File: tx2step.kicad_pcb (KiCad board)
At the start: 2 copper layers, 86.4 x 31.8 mm, 60 parts, among them CON1 BARREL_JACK, IC1 TPS2113A, IC3 MCP73831, IC4 TPS61202, IC5 DRV8834, IC6 DRV8834, J1 8P8C, J2 6P4Cx2, J4 Prog, J5 CHASSIS_SWITCHES, SW1 SW_DIP_x02, U1 ATmega328P-MMH, Y1 16 MHz

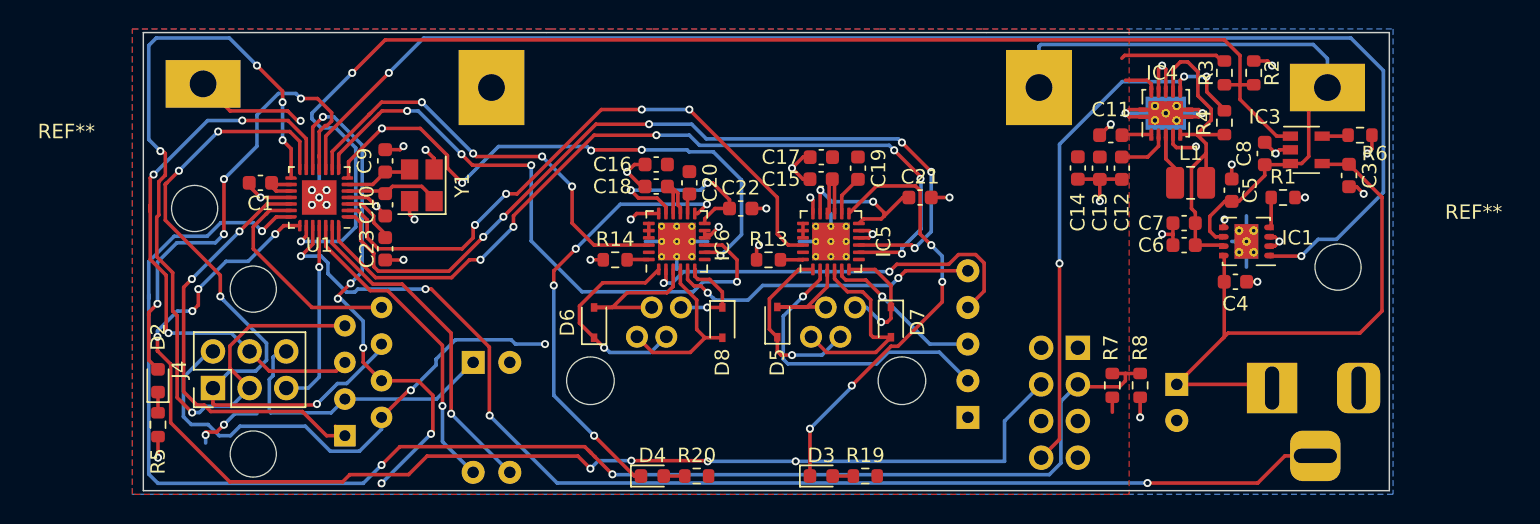
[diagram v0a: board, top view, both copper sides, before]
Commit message: Use trimpots to adjust current clamping
It turns out resistor networks aren't available in a wide variety of
values. Replace the resistor network with fixed value resistors and
add trimpots for each axis to adjust the current clamping.
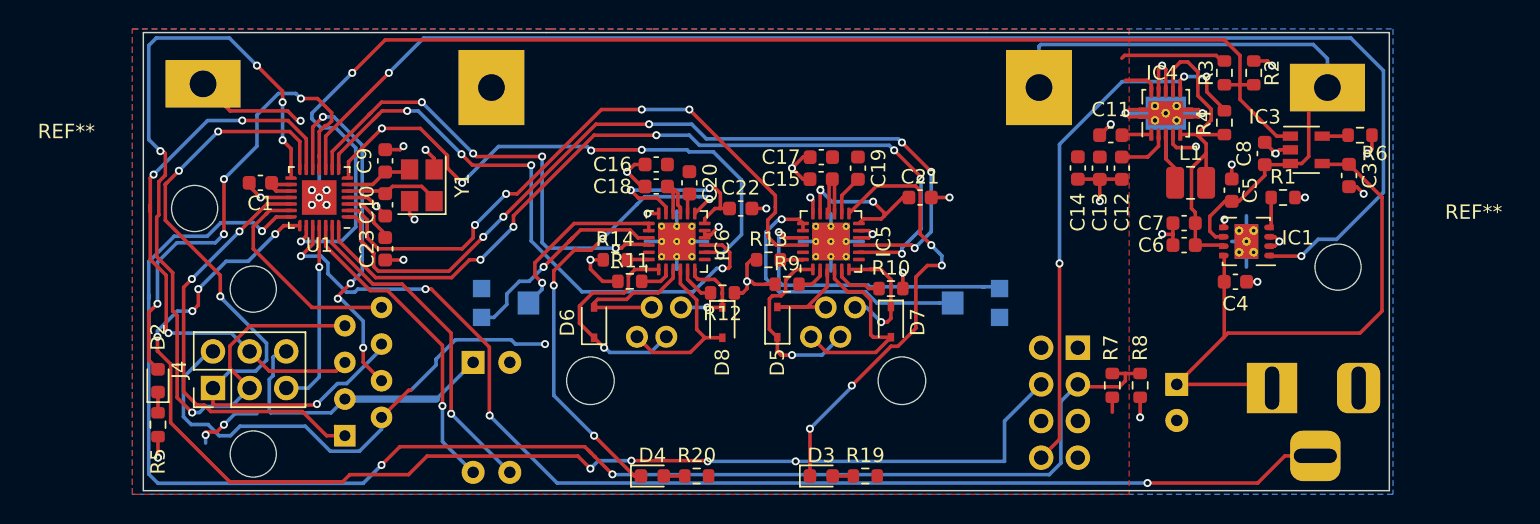
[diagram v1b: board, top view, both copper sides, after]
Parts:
- removed RN1: R_Network04, Resistor_THT:R_Array_SIP5
- added R10: BISEN, Resistor_SMD:R_0603_1608Metric, F.Cu at (160.3, 75.4)
- added R11: AISEN, Resistor_SMD:R_0603_1608Metric, F.Cu at (142.2, 74.9)
- added R12: BISEN, Resistor_SMD:R_0603_1608Metric, F.Cu at (148.6, 75.7)
- added R9: AISEN, Resistor_SMD:R_0603_1608Metric, F.Cu at (153.1, 75.1)
- added RV1: R_POT_TRIM, Potentiometer_SMD:Potentiometer_Bourns_TC33X_Vertical, B.Cu at (166.0, 76.4)
- added RV2: R_POT_TRIM, Potentiometer_SMD:Potentiometer_Bourns_TC33X_Vertical, B.Cu at (133.7, 76.4)
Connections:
- IC5 pad 21: Net-(IC5-Pad19) -> Net-(IC5-Pad21)
- IC6 pad 21: Net-(IC6-Pad19) -> Net-(IC6-Pad21)
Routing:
- net Net-(IC6-Pad2): track 27.8 -> 2.29 mm, vias 2 -> 0
- net Net-(IC5-Pad21): track 0.00 -> 20.9 mm, vias 0 -> 1
- net Net-(IC5-Pad19): track 1.00 -> 20.4 mm, vias 0 -> 1
- net Net-(IC5-Pad2): track 21.4 -> 2.16 mm, vias 1 -> 0
- net Net-(IC6-Pad5): track 21.6 -> 3.13 mm, vias 2 -> 0
- net Net-(IC6-Pad21): track 0.00 -> 15.1 mm, vias 0 -> 1
- net GND: track 124.4 -> 138.4 mm, vias 42 -> 43
- net Net-(IC6-Pad19): track 1.00 -> 12.9 mm, vias 0 -> 1
- net /ST4_RA+: track 37.7 -> 26.0 mm, vias 6 -> 4
- net Net-(IC5-Pad5): track 11.2 -> 3.43 mm, vias 1 -> 0
- net /DEC_PWR: track 30.4 -> 32.6 mm
- net /DEC_DIR: track 43.2 -> 41.9 mm
- net Net-(D4-Pad1): track 30.6 -> 31.6 mm
- net /RA_PWR: track 43.2 -> 44.2 mm
- net Net-(D7-Pad1): track 8.67 -> 9.44 mm
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
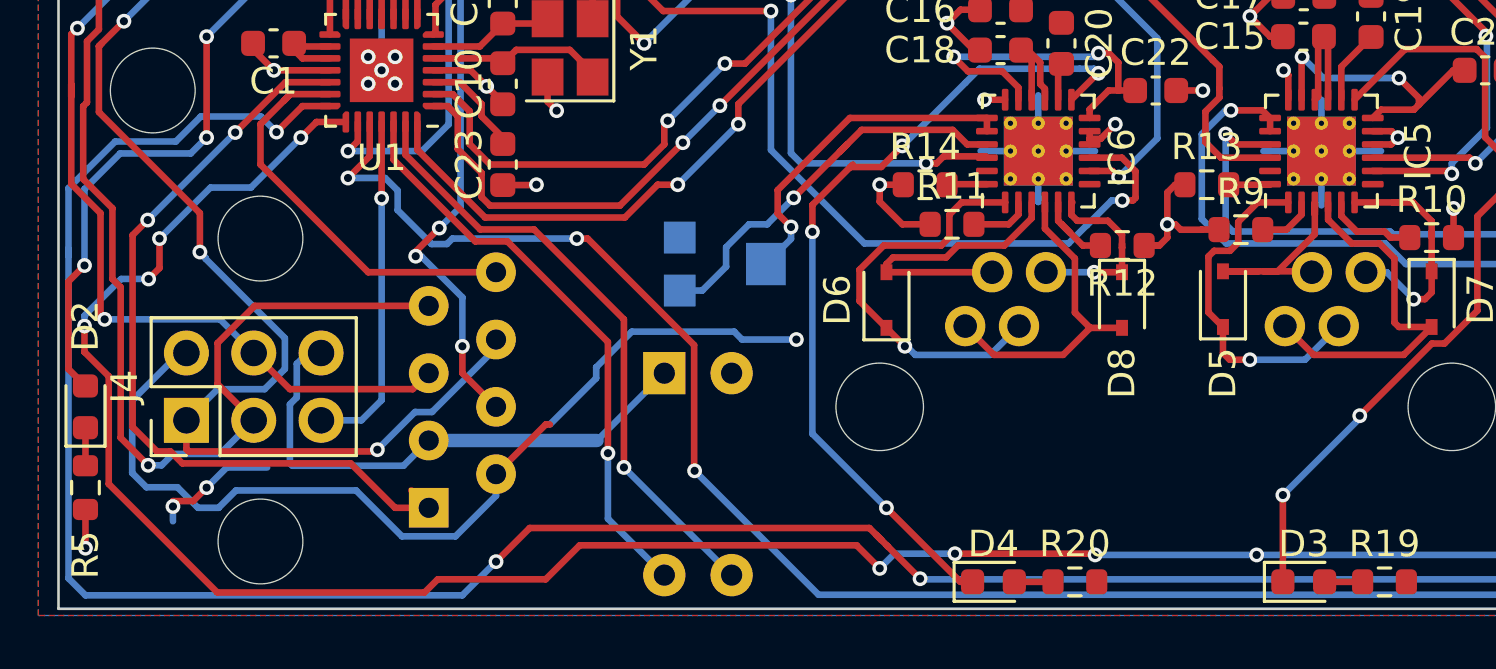
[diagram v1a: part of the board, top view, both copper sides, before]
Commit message: Fix up silkscreen collisions
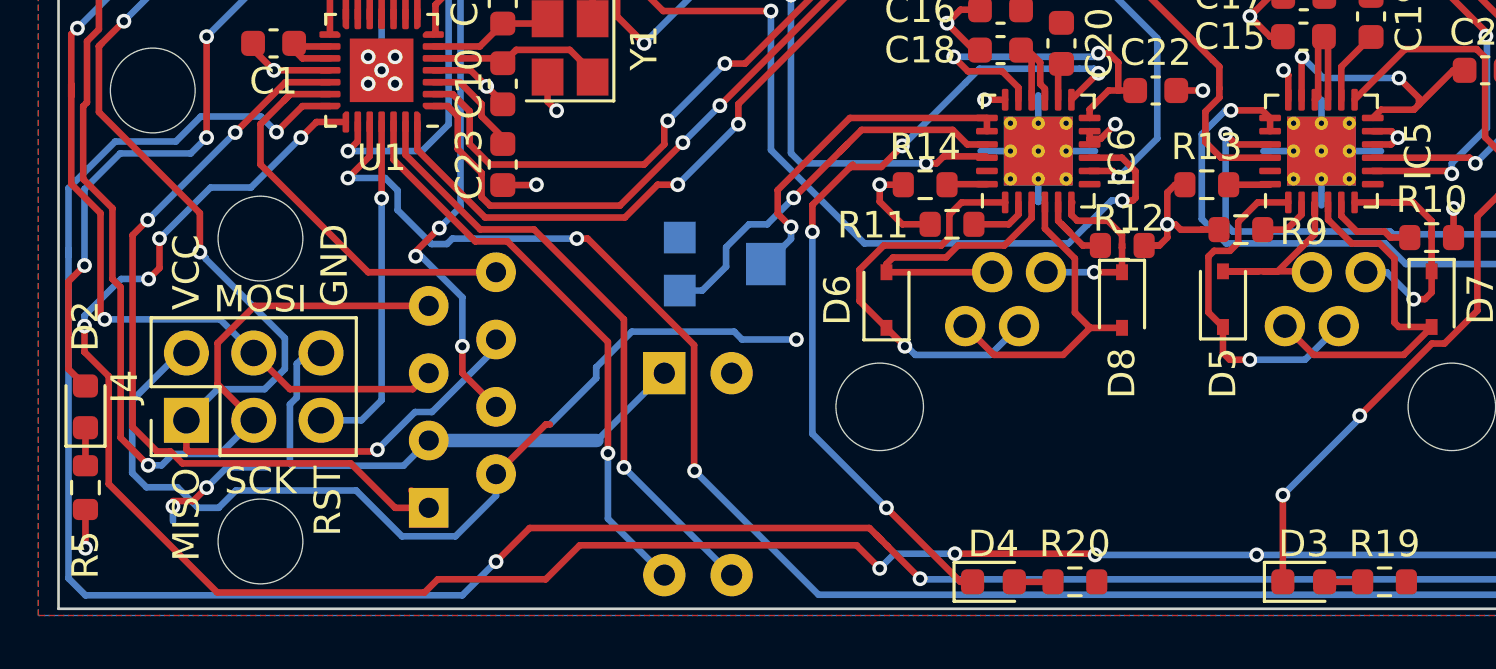
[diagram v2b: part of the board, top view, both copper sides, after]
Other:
- board text added: "GND"
- board text added: "MISO"
- board text added: "MOSI"
- board text added: "RST"
- board text added: "SCK"
- board text added: "VCC"

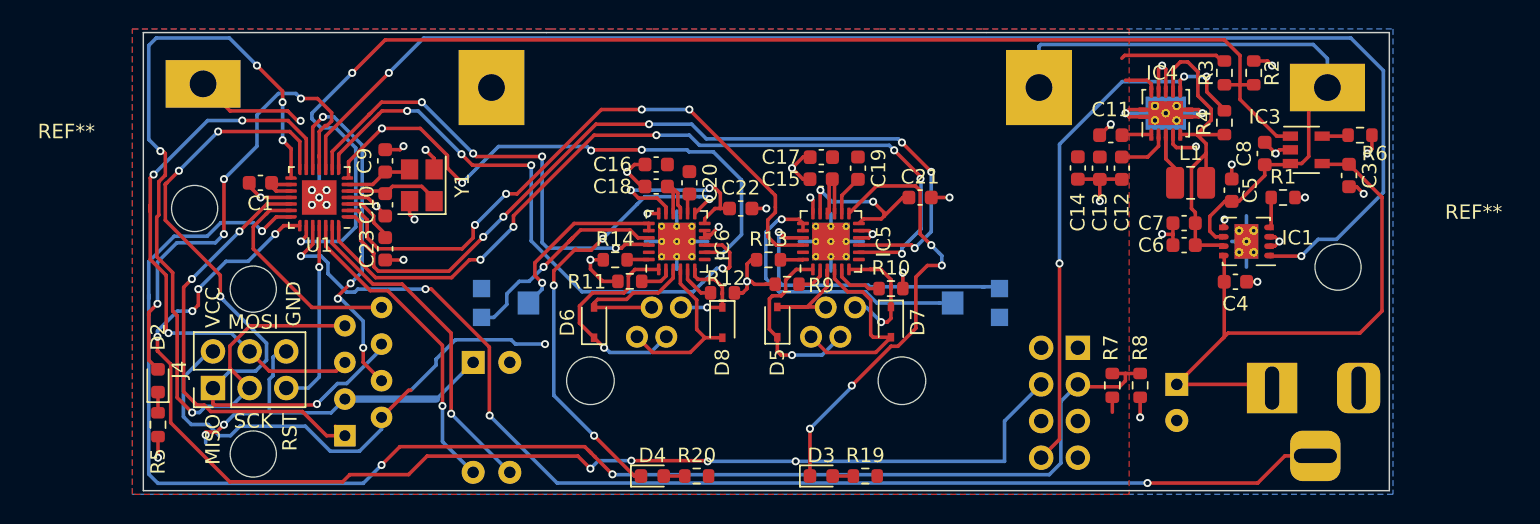
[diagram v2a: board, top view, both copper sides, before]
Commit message: Add more power planes
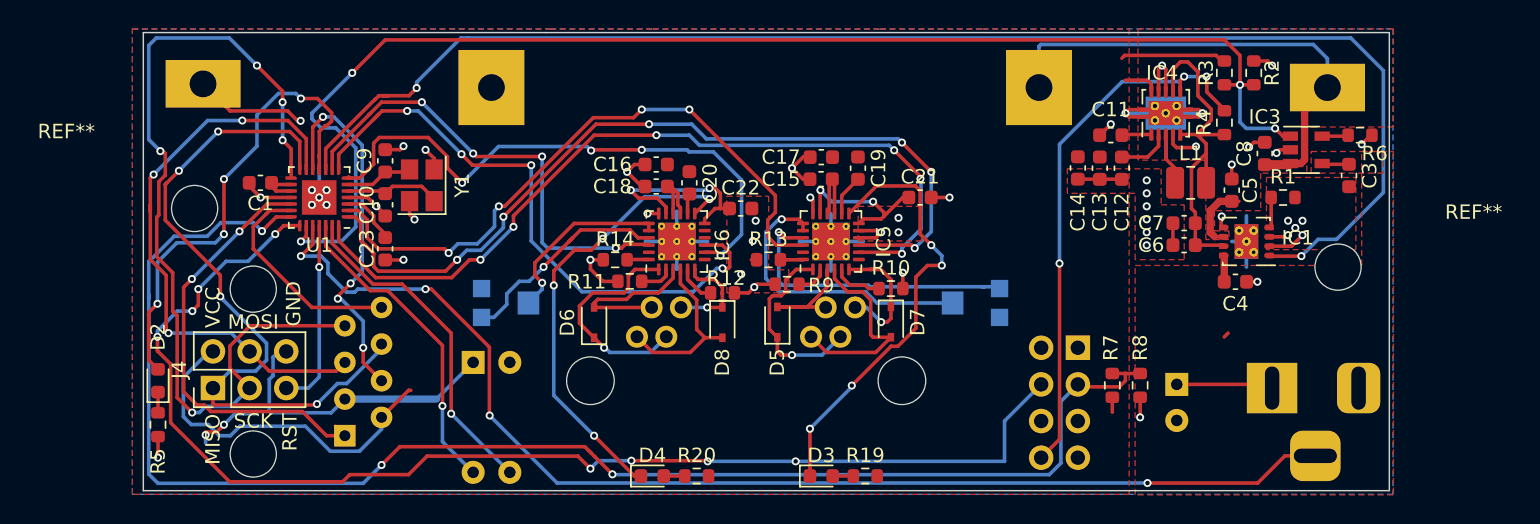
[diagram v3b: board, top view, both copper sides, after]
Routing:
- net +5V: track 41.9 -> 10.8 mm
- net VCC: track 67.2 -> 56.1 mm, vias 1 -> 0
- net GND: track 138.4 -> 132.3 mm, vias 43 -> 53
- net Net-(BT1-Pad1): track 44.1 -> 42.8 mm
- net /CHARGE_STAT: track 91.7 -> 92.6 mm, vias 2 -> 4
- net /DEC_STEP: track 40.5 -> 40.3 mm, vias 5 -> 4
- added copper zone on F.Cu, net +5V
- added copper zone on F.Cu, net GND
- added copper zone on F.Cu, net Net-(BT1-Pad1)

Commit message: Rotate DIP switch
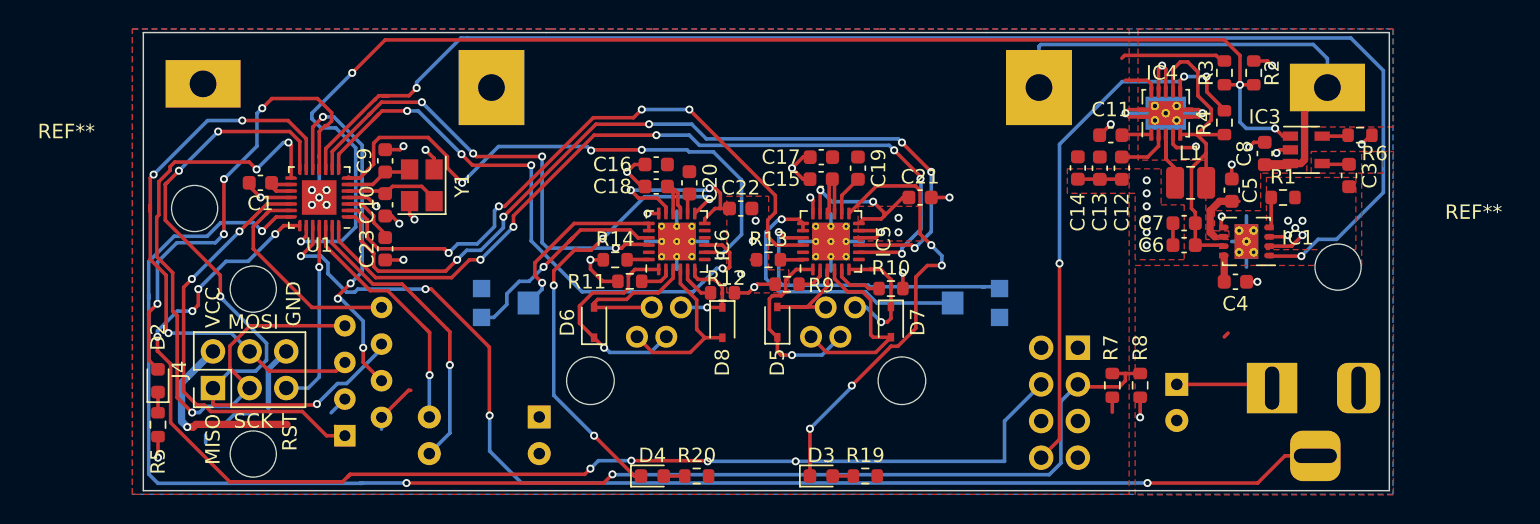
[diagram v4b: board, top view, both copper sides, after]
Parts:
- moved SW1 5.94 mm to (135.9, 84.3), turned to 180 degrees
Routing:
- net GND: track 132.3 -> 109.4 mm, vias 53 -> 51
- net /ST4_RA-: track 61.4 -> 47.0 mm, vias 5 -> 3
- net VCC: track 56.1 -> 48.2 mm, vias 0 -> 1
- net /DIP1: track 22.0 -> 17.3 mm
- net /DIP2: track 23.4 -> 21.0 mm
- net /TRACK_RATE: track 104.5 -> 102.8 mm
- net /DC_SENSE: track 83.4 -> 84.9 mm
- net /GUIDE_RATE: track 87.6 -> 87.1 mm

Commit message: Renumber references
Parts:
- renumbered C23 to C1, C9 to C11, C11 to C12, C12 to C13, C13 to C14, C14 to C15, C15 to C16, C16 to C17, C17 to C18, C18 to C19, C3 to C2, C19 to C20, C20 to C21, C21 to C22, C22 to C23, C2 to C3, C1 to C5, C5 to C6, C6 to C7, C7 to C8, C8 to C9, D2 to D1, D3 to D2, D4 to D3, D5 to D4, D6 to D5, D7 to D6, D8 to D7, IC3 to IC2, IC4 to IC3, IC5 to IC4, IC6 to IC5, J4 to J1, J1 to J2, J5 to J3, J2 to J4, R14 to R10, R9 to R11, R10 to R12, R11 to R13, R12 to R14, R19 to R15, R20 to R16, R5 to R4, R4 to R5, R13 to R9

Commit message: Update silkscreen revision ID
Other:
- board text added: "Texas Two Step rev. 0.1 αLyraen Astronomy"
- board text removed: "Texas Two Step rev. 0 αLyraen Astronomy"
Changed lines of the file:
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@@
     (effects (font (size 1 1) (thickness 0.15)))
   )
-  (gr_text "Texas Two Step rev. 0\nαLyraen Astronomy" (at 178.816 73.914) (layer B.SilkS)
+  (gr_text "Texas Two Step rev. 0.1\nαLyraen Astronomy" (at 178.816 73.914) (layer B.SilkS)
     (effects (font (size 1 1) (thickness 0.15)) (justify mirror))
   )

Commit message: Clean up tracks
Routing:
- net Net-(BT1-Pad1): track 42.8 -> 20.0 mm
- net /DEC_PWR: track 32.6 -> 29.2 mm, vias 4 -> 2
- net /RA_STEP: track 57.1 -> 60.4 mm, vias 6 -> 2
- net /CHARGE_STAT: track 92.6 -> 95.9 mm
- net VCC: track 48.2 -> 45.0 mm, vias 1 -> 0
- net /DEC_DIR: track 41.9 -> 38.8 mm, vias 4 -> 2
- net /JS_RA: track 30.4 -> 33.2 mm, vias 2 -> 4
- net /GUIDE_RATE: track 87.1 -> 89.8 mm, vias 8 -> 5
- net GND: track 109.4 -> 111.6 mm, vias 51 -> 48
- net /RA_PWR: track 44.6 -> 46.8 mm, vias 4 -> 2
- net Net-(D4-Pad2): track 8.84 -> 10.9 mm
- net /DC_SENSE: track 84.9 -> 83.0 mm, vias 4 -> 1
- net Net-(D2-Pad1): track 31.0 -> 29.4 mm, vias 4 -> 2
- net /ST4_RA+: track 26.0 -> 27.5 mm, vias 4 -> 1
- net Net-(D7-Pad2): track 12.2 -> 13.7 mm
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
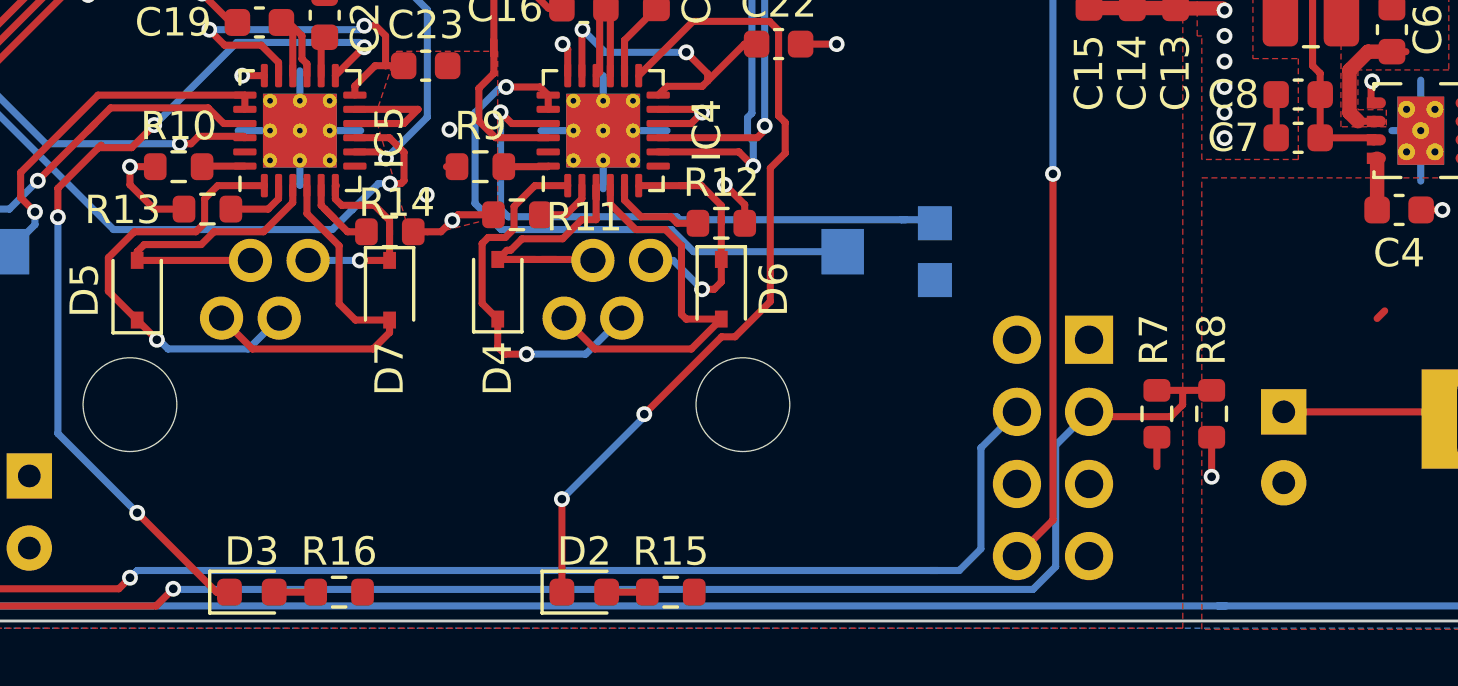
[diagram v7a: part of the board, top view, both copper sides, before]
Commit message: Rotate switch headers
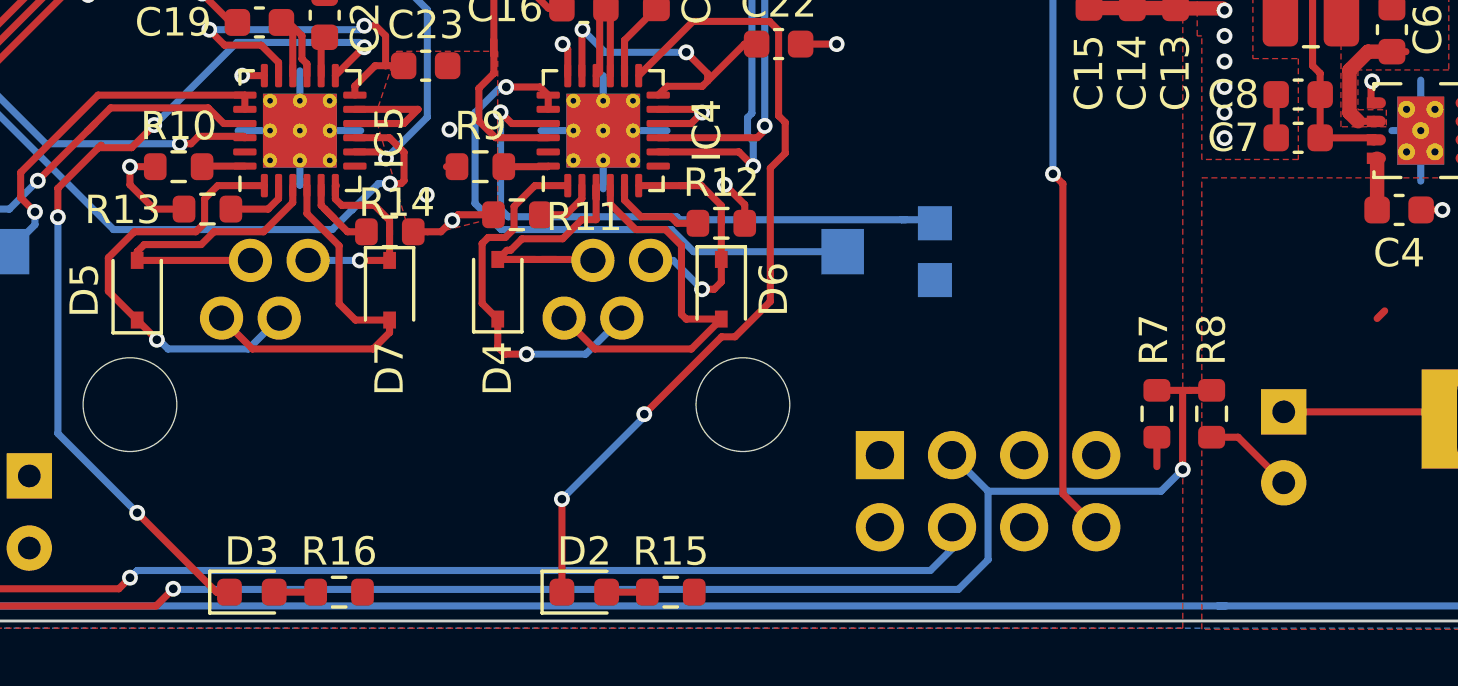
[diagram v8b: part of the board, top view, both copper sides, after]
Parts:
- moved J3 8.41 mm to (165.9, 83.6), turned to 270 degrees
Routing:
- net /GUIDE_RATE: track 89.8 -> 83.9 mm
- net /TRACK_RATE: track 102.9 -> 104.8 mm, vias 3 -> 4
- net GND: track 111.6 -> 113.4 mm, vias 48 -> 47
- net /SW_POWER: track 38.4 -> 37.5 mm
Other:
- board text added: "GUIDE RATE"
- board text added: "POWER"
- board text added: "TRACK RATE"
